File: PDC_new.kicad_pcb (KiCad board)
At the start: 2 copper layers, 156.5 x 145.5 mm, 81 parts, among them J1 Conn_01x02_Pin, J10 Conn_01x02_Pin, J11 XT90PW(2+2)-M.G.Y, J12 Conn_01x02_Pin, J13 XT90PW-F, J2 Conn_01x02_Pin, J3 Conn_01x02_Pin, J4 Conn_01x02_Pin, J5 Conn_01x02_Pin, J6 Conn_01x02_Pin, J7 Conn_01x02_Pin, J8 Conn_01x02_Pin, J9 Conn_01x02_Pin, Q2 IRF540NSTRLPBF, U1 TPSI3050QDWZRQ1, U10 LM393LVDR, U11 IPB017N10N5ATMA1, U12 IPB017N10N5ATMA1, U14 IPB017N10N5ATMA1, U2 TPSI3050QDWZRQ1, U4 74HC74, U5 URB4805LD-60WR3, U6 IPB017N10N5ATMA1, U7 TLC555CDR, U8 SN74HC08D, U9 SN74HC14DR

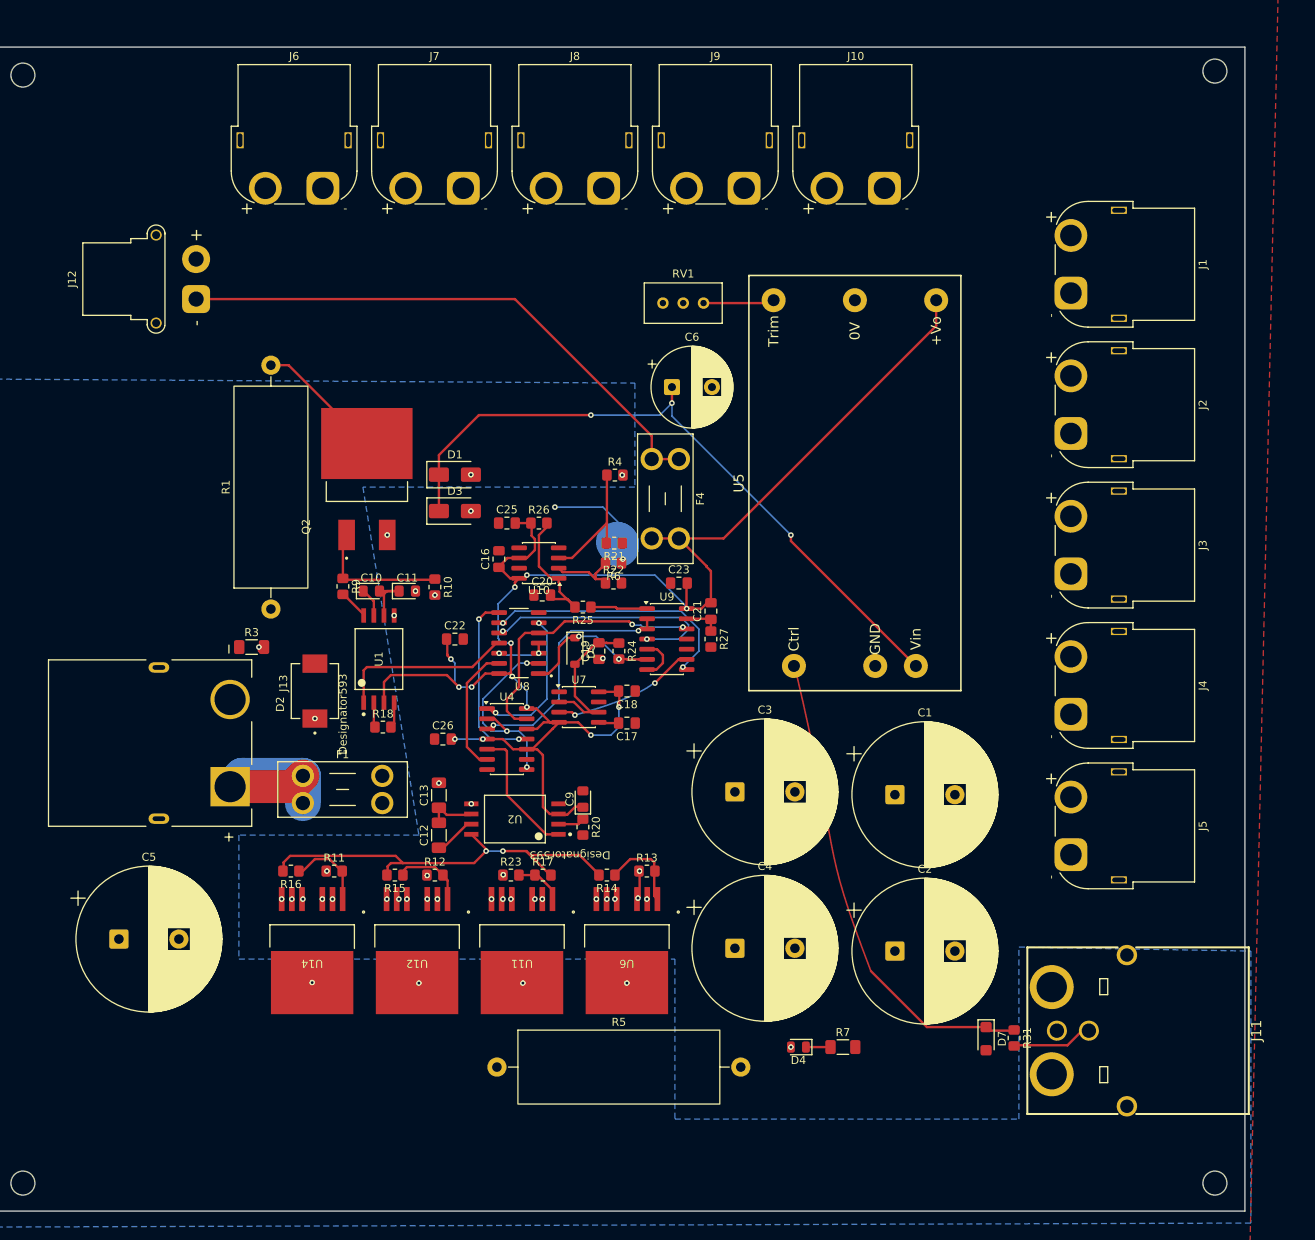
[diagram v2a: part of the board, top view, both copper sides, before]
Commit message: Update PDC_new PCB layout with latest local changes
Replace PDC_new.kicad_pcb with the latest locally saved board. Adds two
AMASS XT60PW-F connector footprints (10 -> 12) along with the related
layout edits.

Co-Authored-By: Claude Opus 5.5 <noreply@anthropic.com>
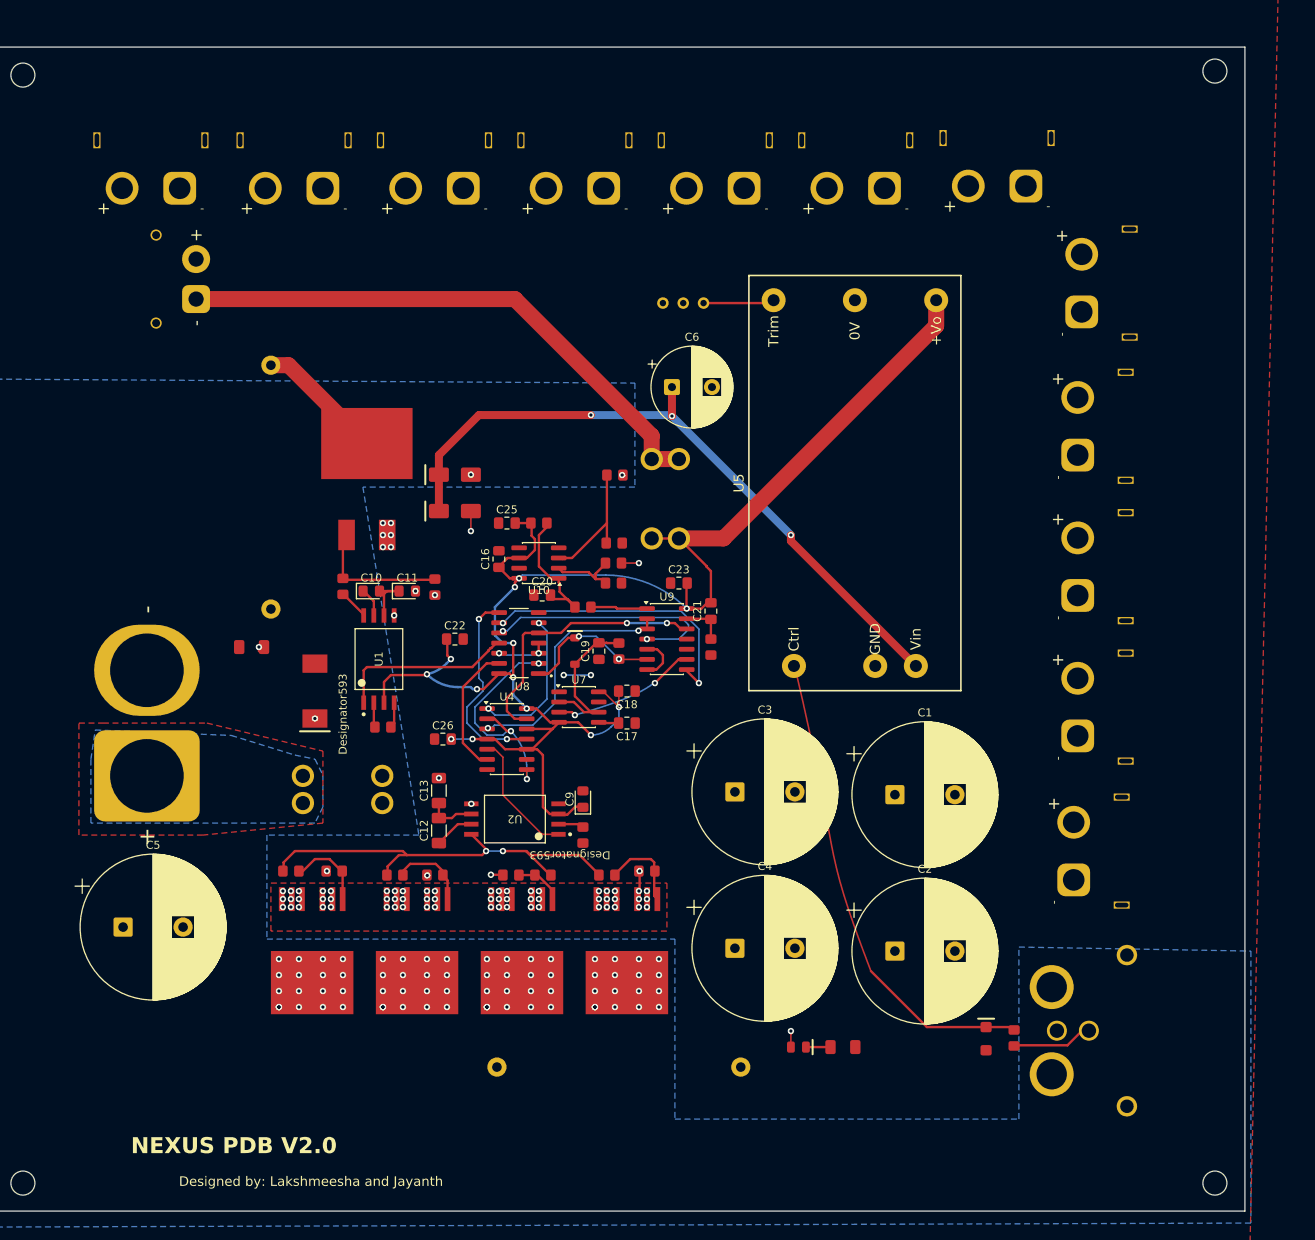
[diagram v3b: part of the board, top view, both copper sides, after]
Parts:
- added J14: Conn_01x02_Pin, Connector_AMASS:AMASS_XT60PW-F_1x02_P7.20mm_Horizontal, F.Cu at (361.9, 144.4)
- added J15: Conn_01x02_Pin, Connector_AMASS:AMASS_XT60PW-F_1x02_P7.20mm_Horizontal, F.Cu at (256.1, 144.7)
- J13: value XT90PW-F -> Conn_01x02_Pin; footprint XT90PW-F:AMASS_XT90PW-F -> QS8_S_Connectors:QS8-S-M_Vertical_DirectCup
- R5: value 1k -> 10k
- moved J5 3.17 mm to (367.9, 231.1)
- moved J13 2.92 mm to (252.0, 211.5), turned to 90 degrees
- moved J3 2.83 mm to (368.4, 195.6)
- moved J2 2.83 mm to (368.4, 178.0)
- moved J4 2.83 mm to (368.4, 213.1)
- moved J1 2.71 mm to (368.9, 160.1)
- moved C5 1.59 mm to (249.0, 237.0)
- moved R20 1.00 mm to (306.5, 225.5)
- moved R27 1.00 mm to (322.5, 202.0)
- moved C12 0.59 mm to (288.5, 224.9)
- moved C13 0.59 mm to (288.5, 219.9)
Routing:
- net /BATT_IN: track 22.8 -> 4.81 mm
- net /FAULT_N: track 25.1 -> 28.9 mm
- net GND: track 8.98 -> 12.2 mm, vias 1 -> 2
- net /BUS+: track 18.6 -> 15.6 mm, vias 34 -> 78
- net /TIMEOUT: track 32.9 -> 35.6 mm
- net /BATT+: track 3.89 -> 1.21 mm, vias 8 -> 72
- net /FAULT_SET: track 23.0 -> 25.2 mm
- net /+5V: track 204.8 -> 203.0 mm
- net /MSTR_ON: track 19.3 -> 18.3 mm
- net /reset_rc: track 4.67 -> 5.58 mm
- net /GATE_U12: track 9.40 -> 10.1 mm
- net /GATE_MAIN: track 53.4 -> 54.0 mm
- net /BUCK_IN: track 86.3 -> 85.7 mm
- net /reset_N: track 35.1 -> 34.6 mm
- added copper zone on B.Cu, net /BATT_IN
- added copper zone on F.Cu, net /BATT_IN
- added copper zone on F.Cu, net /BUS+
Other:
- board text added: "Designed by: Lakshmeesha and Jayanth"
- board text added: "NEXUS PDB V2.0"
